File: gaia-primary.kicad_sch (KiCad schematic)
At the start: 3 parts, among them U1 BME680/BME690, U2 Gaia Connector A, U3 Gaia Connector B

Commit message: adding components
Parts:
- added C1, C2, C3, C4: 1uF, Capacitor_SMD:C_0402_1005Metric, symbol Device:C_Small
- added C10, C13: 10nF, Capacitor_SMD:C_0603_1608Metric, symbol Device:C_Small
- added C11, C12, C8, C9: 100nF, Capacitor_SMD:C_0603_1608Metric, symbol Device:C_Small
- added JP1: SolderJumper_3_Open, Jumper:SolderJumper-3_P2.0mm_Open_TrianglePad1.0x1.5mm, symbol Jumper:SolderJumper_3_Open
- added R12, R13: 4kOhm 0,1%, Resistor_SMD:R_1206_3216Metric, symbol Device:R_Small
- added TH1, TH2: Pt1000, cs25_onionsat:yageo_m1020, symbol Sensor_Temperature:PT1000
- added U10: AP2112K-1.8, Package_TO_SOT_SMD:SOT-23-5, symbol Regulator_Linear:AP2112K-1.8
- added U11: AP2112K-3.3, Package_TO_SOT_SMD:SOT-23-5, symbol Regulator_Linear:AP2112K-3.3
- added U4: STM32F103C8Tx, Package_QFP:LQFP-48_7x7mm_P0.5mm, symbol MCU_ST_STM32F1:STM32F103C8Tx
- added U5, U7: ICM-20948, Sensor_Motion:InvenSense_QFN-24_3x3mm_P0.4mm, symbol Sensor_Motion:ICM-20948
- added U6: BME680/BME690, Package_LGA:Bosch_LGA-8_3x3mm_P0.8mm_ClockwisePinNumbering, symbol Sensor:BME680
- added U8, U9: MAX31865xTP, Package_DFN_QFN:TQFN-20-1EP_5x5mm_P0.65mm_EP3.1x3.1mm, symbol Sensor_Temperature:MAX31865xTP
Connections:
- net GND: now also C1.2, C11.1, C12.2, C2.2, C3.2, C4.2, C8.1, C9.2, U10.2 (GND), U11.2 (GND), U6.1 (GND), U6.7 (GND), U8.10 (GND), U8.15 (DGND), U8.16 (GND), U8.21 (GND), U8.6 (FORCE2), U9.10 (GND), U9.15 (DGND), U9.16 (GND), U9.21 (GND), U9.6 (FORCE2)
- net VOUT_A1: now also JP1.1 (A)
- net VOUT_B1: now also JP1.3 (B)
- net VOUT_A2: no longer names the net of U2.3 (VOUT_A2)
- net VOUT_A2: no longer U2.4 (VOUT_A2)
- net VOUT_A3: no longer names the net of U2.5 (VOUT_A3)
- net VOUT_A3: no longer U2.6 (VOUT_A3)
- net VOUT_B2: no longer names the net of U2.10 (VOUT_B2)
- net VOUT_B2: no longer U2.9 (VOUT_B2)
- new net: R12.1, U8.1 (BIAS), U8.2 (REFIN+)
- new net: R12.2, U8.3 (REFIN-), U8.4 (ISENSOR)
- new net: C10.1, TH1.1, U8.5 (FORCE+), U8.7 (RTDIN+)
- new net: C10.2, TH1.2, U8.8 (RTDIN-), U8.9 (FORCE-)
- new net: U5.18 (GND), U5.20 (GND)
- new net: C13.1, TH2.1, U9.5 (FORCE+), U9.7 (RTDIN+)
- new net: C13.2, TH2.2, U9.8 (RTDIN-), U9.9 (FORCE-)
- new net: U4.23 (VSS), U4.35 (VSS), U4.47 (VSS)
- new net: U7.18 (GND), U7.20 (GND)
- new net: R13.1, U9.1 (BIAS), U9.2 (REFIN+)
- new net: R13.2, U9.3 (REFIN-), U9.4 (ISENSOR)
- new net +1V8: C4.1, U10.5 (VOUT)
- new net +3.3V: C11.2, C12.1, C2.1, C8.2, C9.1, U11.5 (VOUT), U8.19 (DVDD), U8.20 (VDD), U9.19 (DVDD), U9.20 (VDD)
- new net CS2: U9.13 (~{CS})
- new net DRDY: U8.18 (~{DRDY}), U9.18 (~{DRDY})
- new net SCLK: U9.12 (SCLK)
- new net SDI: U9.11 (SDI)
- new net SDO: U9.14 (SDO)
- new net VCC: C1.1, C3.1, JP1.2 (C), U10.1 (VIN), U10.3 (EN), U11.1 (VIN), U11.3 (EN)
- no-connect marks 0 -> 6
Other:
- moved on the sheet: U1

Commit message: Adding Bosch BME690, TDK ICM-20948, Maxim MAX31865 ICs
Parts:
- removed R12: 4kOhm 0,1%, Resistor_SMD:R_1206_3216Metric, symbol Device:R_Small
- removed U6: BME680/BME690, Package_LGA:Bosch_LGA-8_3x3mm_P0.8mm_ClockwisePinNumbering, symbol Sensor:BME680
- removed U8: MAX31865xTP, Package_DFN_QFN:TQFN-20-1EP_5x5mm_P0.65mm_EP3.1x3.1mm, symbol Sensor_Temperature:MAX31865xTP
- added C14, C15, C16, C17, C18, C19, C20, C5, C6, C7: 100nF, Capacitor_SMD:C_0402_1005Metric, symbol Device:C_Small
- added Q1, Q2: BSS138, Package_TO_SOT_SMD:SOT-23, symbol Transistor_FET:BSS138
- added R1, R2, R3, R4, R5, R6, R8, R9: 10k, Resistor_SMD:R_0402_1005Metric, symbol Device:R_Small
- added R7: 4kOhm 0,1%, Resistor_SMD:R_1206_3216Metric, symbol Device:R_Small
- added U6: MAX31865xTP, Package_DFN_QFN:TQFN-20-1EP_5x5mm_P0.65mm_EP3.1x3.1mm, symbol Sensor_Temperature:MAX31865xTP
- added U8: BME680/BME690, Package_LGA:Bosch_LGA-8_3x3mm_P0.8mm_ClockwisePinNumbering, symbol Sensor:BME680
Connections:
- net +1V8: now also U5.13 (VDD), U5.8 (VDDIO), U7.13 (VDD), U7.8 (VDDIO), U7.9 (SDO/AD0), C14.2, C15.2, C5.2, C6.2, Q1.1 (G), Q2.1 (G), R1.1, R4.1
- net +3.3V: now also U1.2 (CSB), U1.6 (VDDIO), U1.8 (VDD), C17.2, C18.2, C19.2, C20.2, R2.1, R3.1, R5.1, R6.1, R8.1, R9.1, U6.19 (DVDD), U6.20 (VDD), U8.2 (CSB), U8.5 (SDO), U8.6 (VDDIO), U8.8 (VDD)
- net GND: now also U1.5 (SDO), U5.18 (GND), U5.20 (GND), U5.9 (SDO/AD0), U7.18 (GND), U7.20 (GND), C14.1, C15.1, C16.1, C17.1, C18.1, C19.1, C20.1, C5.1, C6.1, C7.1, U6.10 (GND), U6.15 (DGND), U6.16 (GND), U6.21 (GND), U6.6 (FORCE2), U8.1 (GND), U8.7 (GND)
- net at C10.1, TH1.1: now also U6.5 (FORCE+), U6.7 (RTDIN+)
- net at C10.2, TH1.2: now also U6.8 (RTDIN-), U6.9 (FORCE-)
- net at U5.10 (REGOUT): now also C16.2
- net SCL_1V8: now reaches U5.23 (SCL/SCLK)
- net SCL_1V8: now also U7.23 (SCL/SCLK), Q1.2 (S), R1.2
- net SDA_1V8: now reaches U5.24 (SDA/SDI)
- net SDA_1V8: now also U7.24 (SDA/SDI), Q2.2 (S), R4.2
- net LOCAL_SDA: now reaches U1.3 (SDI)
- net LOCAL_SDA: now also Q2.3 (D), R3.2, R6.2, R9.2, U8.3 (SDI)
- net LOCAL_SCL: now reaches U1.4 (SCK)
- net LOCAL_SCL: now also Q1.3 (D), R2.2, R5.2, R8.2, U8.4 (SCK)
- net at U7.10 (REGOUT): now also C7.2
- net CS2 renamed LOCAL_CS_2
- net DRDY renamed LOCAL_RD_2
- net SCLK renamed LOCAL_SCLK
- net LOCAL_SCLK: now also U6.12 (SCLK)
- net SDI renamed LOCAL_MOSI
- net LOCAL_MOSI: now also U6.11 (SDI)
- net SDO renamed LOCAL_MISO
- net LOCAL_MISO: now also U6.14 (SDO)
- new net: R7.1, U6.1 (BIAS), U6.2 (REFIN+)
- new net: R7.2, U6.3 (REFIN-), U6.4 (ISENSOR)
- new net LOCAL_CS_1: U6.13 (~{CS})
- new net LOCAL_RD_1: U6.18 (~{DRDY})
- no-connect marks 6 -> 16
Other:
- moved on the sheet: C1, C11, C12, C13, C2, C3, C4, JP1, R13, TH2, U1, U10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

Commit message: Adding ADI ADXL375 + Creating hierarchical sheets
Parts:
- removed C10, C13: 10nF, Capacitor_SMD:C_0603_1608Metric, symbol Device:C_Small
- removed C11, C12, C8, C9: 100nF, Capacitor_SMD:C_0603_1608Metric, symbol Device:C_Small
- removed C14, C15, C16, C17, C18, C19, C20, C5, C6, C7: 100nF, Capacitor_SMD:C_0402_1005Metric, symbol Device:C_Small
- removed R13, R7: 4kOhm 0,1%, Resistor_SMD:R_1206_3216Metric, symbol Device:R_Small
- removed R5, R6, R8, R9: 10k, Resistor_SMD:R_0402_1005Metric, symbol Device:R_Small
- removed TH1, TH2: Pt1000, cs25_onionsat:yageo_m1020, symbol Sensor_Temperature:PT1000
- removed U1, U8: BME680/BME690, Package_LGA:Bosch_LGA-8_3x3mm_P0.8mm_ClockwisePinNumbering, symbol Sensor:BME680
- removed U5, U7: ICM-20948, Sensor_Motion:InvenSense_QFN-24_3x3mm_P0.4mm, symbol Sensor_Motion:ICM-20948
- removed U6, U9: MAX31865xTP, Package_DFN_QFN:TQFN-20-1EP_5x5mm_P0.65mm_EP3.1x3.1mm, symbol Sensor_Temperature:MAX31865xTP
- added JP2, JP3: SolderJumper_3_Open, Jumper:SolderJumper-3_P2.0mm_Open_TrianglePad1.0x1.5mm, symbol Jumper:SolderJumper_3_Open
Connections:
- net I2C_1_SCL: now also JP2.3 (B)
- net I2C_1_SDA: now also JP3.3 (B)
- net I2C_2_SCL: now also JP2.1 (A)
- net I2C_2_SDA: now also JP3.1 (A)
- net LOCAL_SCL: now also JP2.2 (C)
- net LOCAL_SDA: now also JP3.2 (C)
- no-connect marks 16 -> 6
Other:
- added sheet Environmental Sensors (gaia-primary_environmental.kicad_sch)
- added sheet Inertial Measurement Units (gaia-primary_imu.kicad_sch)
- note removed: "Connectors"
- moved on the sheet: C1, C2, C3, C4, JP1, Q1, Q2, R1, R2, R3, R4, U10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

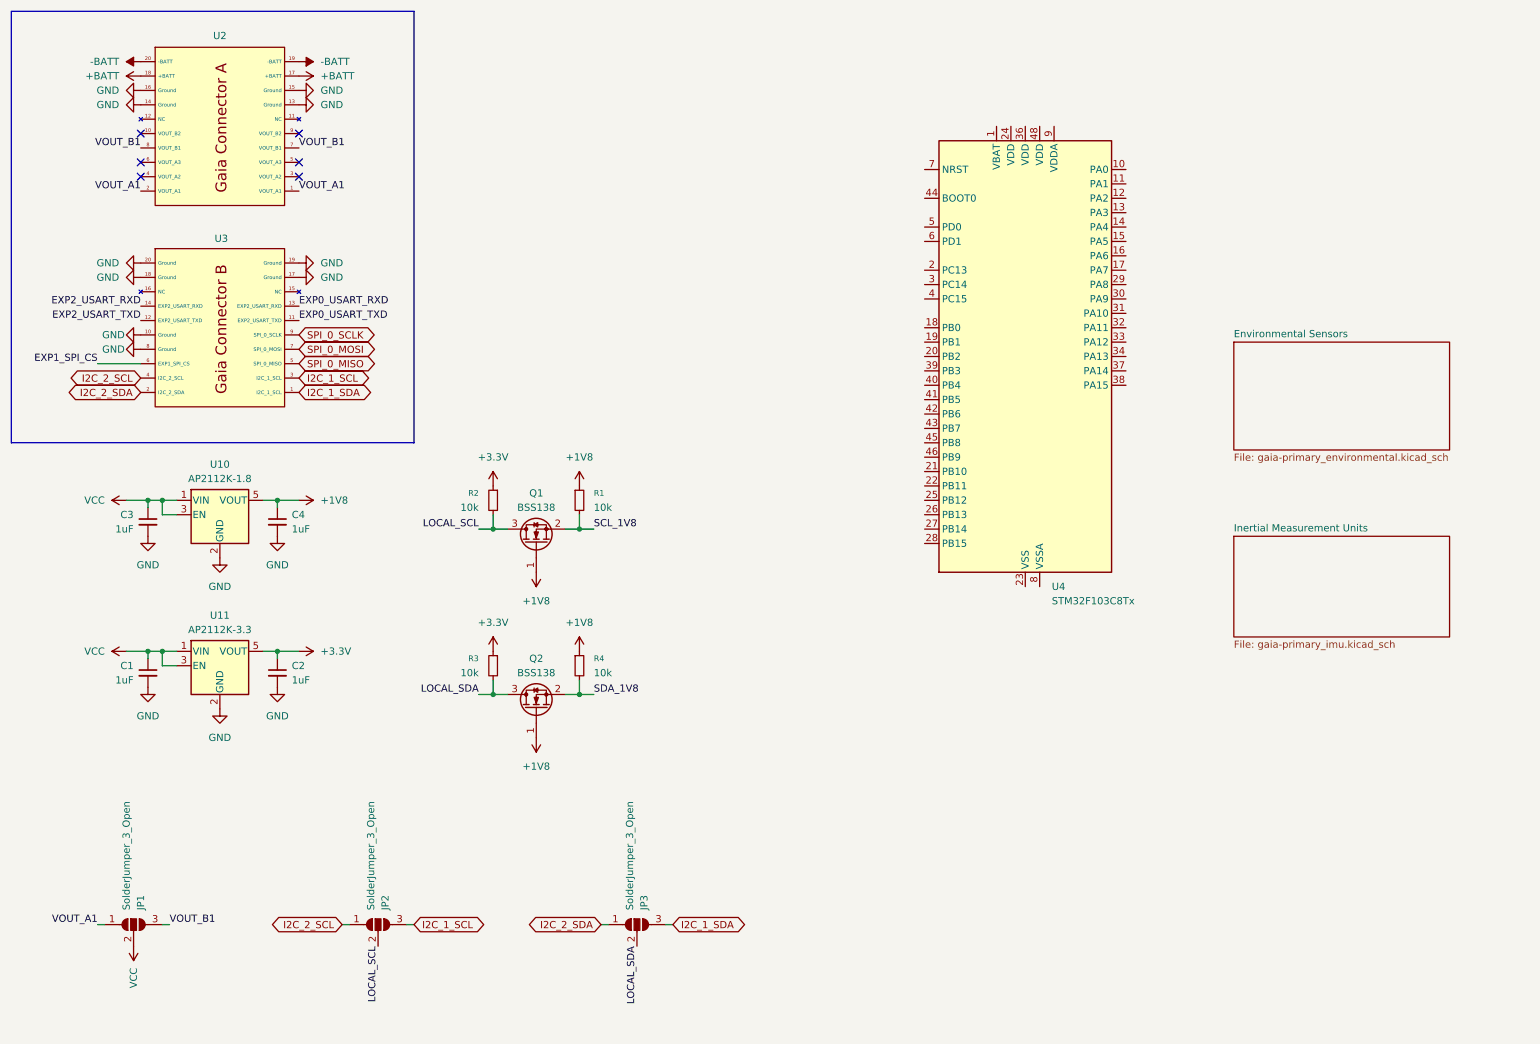
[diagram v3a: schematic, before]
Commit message: Schematic done
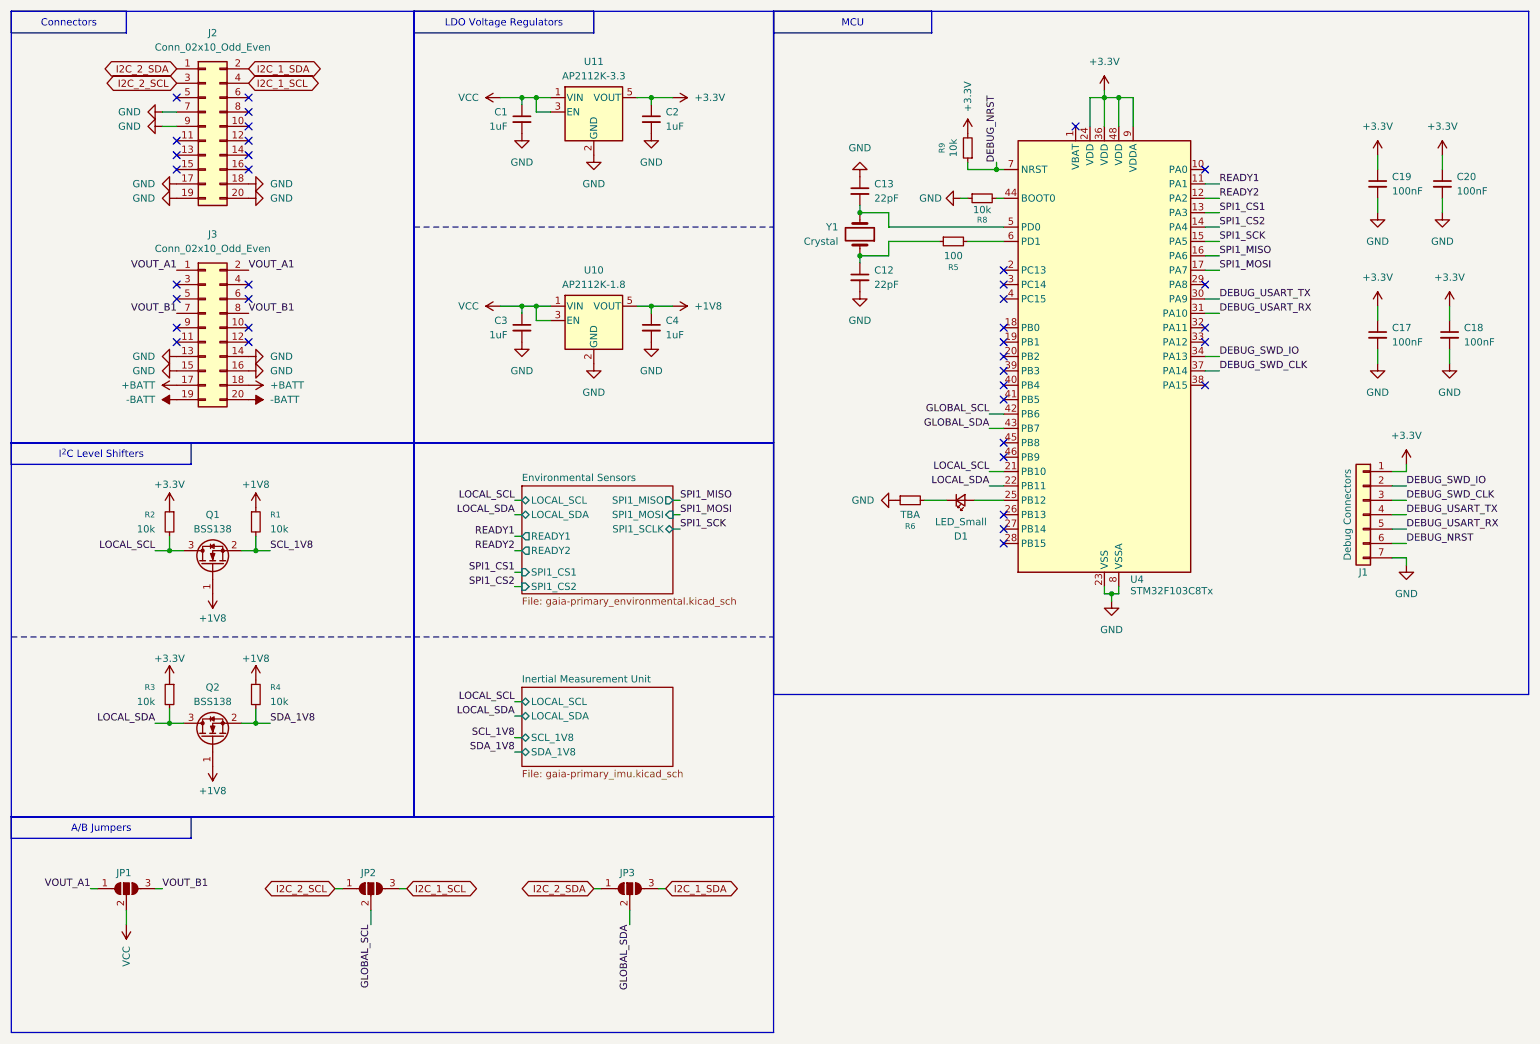
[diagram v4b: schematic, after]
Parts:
- removed U2: Gaia Connector A, gaia-4gmodul-footprints:Gaia_connector_4_6layer, symbol gaia-4gmodul-symbols:gaia-2/4layer-connectorA
- removed U3: Gaia Connector B, gaia-4gmodul-footprints:Gaia_connector_4_6layer, symbol gaia-4gmodul-symbols:gaia-2/4layer-connectorB
- added C12, C13: 22pF, Capacitor_SMD:C_0402_1005Metric, symbol Device:C_Small
- added C17, C18, C19, C20: 100nF, Capacitor_SMD:C_0402_1005Metric, symbol Device:C_Small
- added D1: LED_Small, LED_SMD:LED_0603_1608Metric, symbol Device:LED_Small
- added J1: Debug Connectors, symbol Connector_Generic:Conn_01x07
- added J2, J3: Conn_02x10_Odd_Even, gaia_obc-footprints:PinHeader_2x10_P2.00mm_Vertical_SMD, symbol Connector_Generic:Conn_02x10_Odd_Even
- added R5: 100, Resistor_SMD:R_0402_1005Metric, symbol Device:R_Small
- added R6: TBA, Resistor_SMD:R_0402_1005Metric, symbol Device:R_Small
- added R8, R9: 10k, Resistor_SMD:R_0402_1005Metric, symbol Device:R_Small
- added Y1: Crystal, symbol Device:Crystal
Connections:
- net +3.3V: now also U4.24 (VDD), U4.36 (VDD), U4.48 (VDD), U4.9 (VDDA), C17.1, C18.1, C19.1, C20.1, J1.1 (Pin_1), R9.2
- net +BATT: now also J3.17 (Pin_17), J3.18 (Pin_18)
- net -BATT: now also J3.19 (Pin_19), J3.20 (Pin_20)
- net GND: now also U4.23 (VSS), U4.35 (VSS), U4.47 (VSS), U4.8 (VSSA), C12.2, C13.1, C17.2, C18.2, C19.2, C20.2, J1.7 (Pin_7), J2.17 (Pin_17), J2.18 (Pin_18), J2.19 (Pin_19), J2.20 (Pin_20), J2.7 (Pin_7), J2.9 (Pin_9), J3.13 (Pin_13), J3.14 (Pin_14), J3.15 (Pin_15), J3.16 (Pin_16), R6.1, R8.1
- net I2C_1_SCL: now also J2.4 (Pin_4)
- net I2C_1_SDA: now also J2.2 (Pin_2)
- net I2C_2_SCL: now also J2.3 (Pin_3)
- net I2C_2_SDA: now also J2.1 (Pin_1)
- net LOCAL_SCL: now also U4.21 (PB10); no longer JP2.2 (C)
- net LOCAL_SDA: now also U4.22 (PB11); no longer JP3.2 (C)
- net VOUT_A1: now also J3.1 (Pin_1), J3.2 (Pin_2)
- net VOUT_B1: now also J3.7 (Pin_7), J3.8 (Pin_8)
- net READY1: now reaches U4.11 (PA1)
- net READY2: now reaches U4.12 (PA2)
- net SPI1_CS1: now reaches U4.13 (PA3)
- net SPI1_CS2: now reaches U4.14 (PA4)
- net SPI1_SCK: now reaches U4.15 (PA5)
- net SPI1_MISO: now reaches U4.16 (PA6)
- net SPI1_MOSI: now reaches U4.17 (PA7)
- net at U4.25 (PB12): now also D1.2 (A)
- net DEBUG_USART_TX: now reaches U4.30 (PA9)
- net DEBUG_USART_TX: now also J1.4 (Pin_4)
- net DEBUG_USART_RX: now reaches U4.31 (PA10)
- net DEBUG_USART_RX: now also J1.5 (Pin_5)
- net DEBUG_SWD_IO: now reaches U4.34 (PA13)
- net DEBUG_SWD_IO: now also J1.2 (Pin_2)
- net DEBUG_SWD_CLK: now reaches U4.37 (PA14)
- net DEBUG_SWD_CLK: now also J1.3 (Pin_3)
- net GLOBAL_SCL: now reaches U4.42 (PB6)
- net GLOBAL_SCL: now also JP2.2 (C)
- net GLOBAL_SDA: now reaches U4.43 (PB7)
- net GLOBAL_SDA: now also JP3.2 (C)
- net at U4.44 (BOOT0): now also R8.2
- net at U4.5 (PD0): now also C13.2, Y1.2
- net at U4.6 (PD1): now also R5.2
- net DEBUG_NRST: now reaches U4.7 (NRST)
- net DEBUG_NRST: now also J1.6 (Pin_6), R9.1
- new net: D1.1 (K), R6.2
- new net: C12.1, R5.1, Y1.1
- no-connect marks 6 -> 38
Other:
- sheet Inertial Measurement Units renamed Inertial Measurement Unit
- sheet Environmental Sensors ports: added LOCAL_SCL, LOCAL_SDA, READY1, READY2, SPI1_CS1, SPI1_CS2, SPI1_MISO, SPI1_MOSI, SPI1_SCLK; removed none
- sheet Inertial Measurement Unit ports: added LOCAL_SCL, LOCAL_SDA, SCL_1V8, SDA_1V8; removed none
- moved on the sheet: C1, C2, C3, C4, JP1, JP2, JP3, Q1, Q2, R1, R2, R3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

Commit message: Finalizing PCB, routing
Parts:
- J1: footprint (none) -> gaia-primary-footprints:PinHeader_1x07_P2.54mm_Vertical
- J2, J3: footprint gaia_obc-footprints:PinHeader_2x10_P2.00mm_Vertical_SMD -> gaia-primary-footprints:Gaia_connector_2_4layer
- JP1, JP2, JP3: footprint Jumper:SolderJumper-3_P2.0mm_Open_TrianglePad1.0x1.5mm -> gaia-primary-footprints:SolderJumper-3_P2.0mm_Open_TrianglePad1.0x1.5mm
- Q1, Q2: footprint Package_TO_SOT_SMD:SOT-23 -> gaia-primary-footprints:SOT-23
- U10, U11: footprint Package_TO_SOT_SMD:SOT-23-5 -> gaia-primary-footprints:SOT-23-5
- U4: footprint Package_QFP:LQFP-48_7x7mm_P0.5mm -> gaia-primary-footprints:LQFP-48_7x7mm_P0.5mm
- Y1: footprint (none) -> gaia-primary-footprints:NX3225GD8MHZSTDCRA3
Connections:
- net DEBUG_SWD_CLK: now also J1.2 (Pin_2); no longer J1.3 (Pin_3)
- net DEBUG_SWD_IO: now also J1.3 (Pin_3); no longer J1.2 (Pin_2)
- net DEBUG_USART_RX: now also J1.4 (Pin_4); no longer J1.5 (Pin_5)
- net DEBUG_USART_TX: now also J1.5 (Pin_5); no longer J1.4 (Pin_4)
- net +BATT: no longer names the net of J3.17 (Pin_17)
- net +BATT: no longer J3.18 (Pin_18)
- net -BATT: no longer names the net of J3.19 (Pin_19)
- net -BATT: no longer J3.20 (Pin_20)
- no-connect marks 38 -> 42
